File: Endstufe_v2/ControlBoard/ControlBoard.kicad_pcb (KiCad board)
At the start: 2 copper layers, 67 parts, among them J1 Conn_01x02_Pin, J3 DNP, J7 DNP, SW1 TS-1187A-B-A-B, SW2 TS-1187A-B-A-B, U1 TPS62933, U2 TYPE-C 16PFS 2JCB1.2-H6.5 IPX8, U3 W25Q128JVS, U4 RP2040, U5 NVTFWS014P04M8LTAG, U6 1SMA5927A, U7 ADAU1463WBCPZ300, Y1 12Mhz

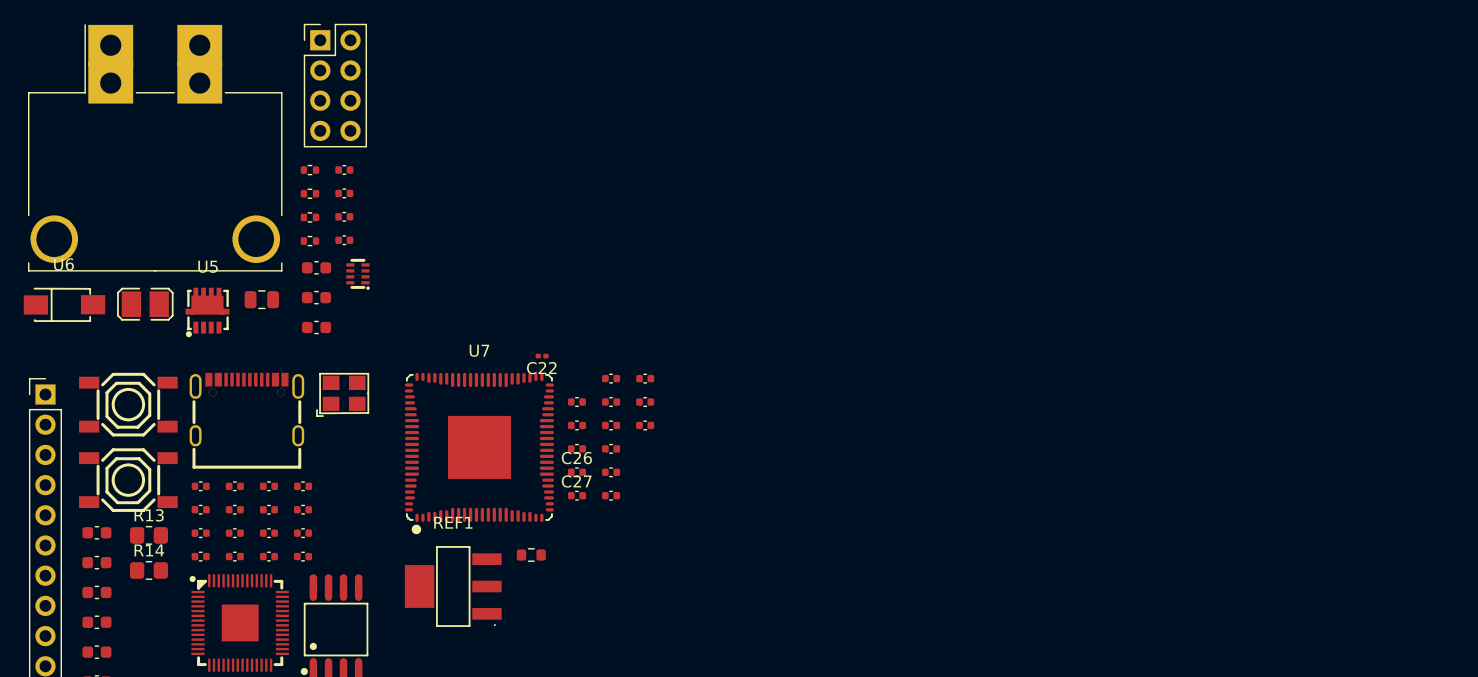
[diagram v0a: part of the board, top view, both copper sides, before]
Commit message: Added ADAU1962A DAC schematic
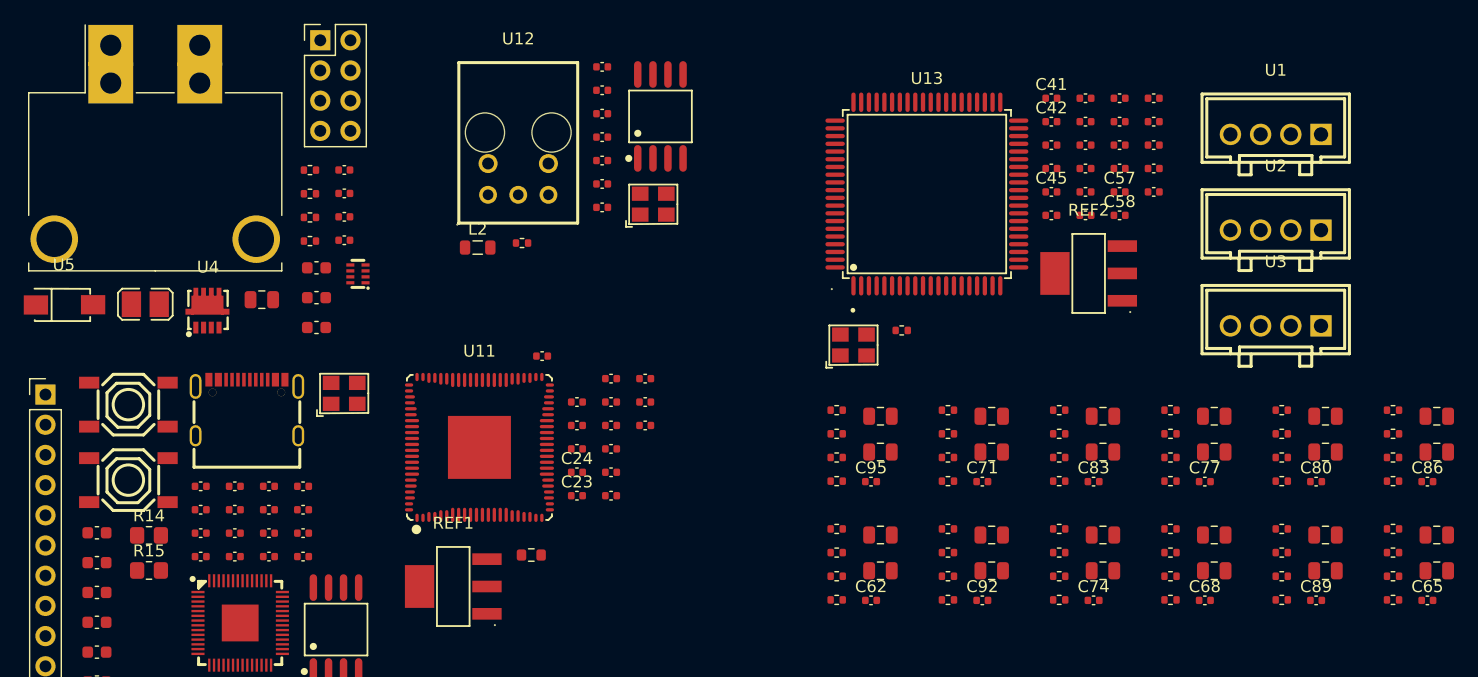
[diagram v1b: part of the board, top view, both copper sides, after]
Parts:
- added C22: 10uF, Endstufe:C_0402_1005Metric, F.Cu at (103.5, 66.6)
- added C25: 30pF, Endstufe:C_0402_1005Metric, F.Cu at (103.5, 62.6)
- added C26: 30pF, Endstufe:C_0402_1005Metric, F.Cu at (103.5, 64.6)
- added C35: 100nF, Endstufe:C_0402_1005Metric, F.Cu at (103.5, 60.7)
- added C41: 470nF, Capacitor_SMD:C_0402_1005Metric, F.Cu at (141.3, 63.3)
- added C42: 470nF, Capacitor_SMD:C_0402_1005Metric, F.Cu at (141.3, 65.3)
- added C43: 30pF, Endstufe:C_0402_1005Metric, F.Cu at (141.3, 67.2)
- added C44: 30pF, Endstufe:C_0402_1005Metric, F.Cu at (141.3, 69.2)
- added C45: 5.6nF, Capacitor_SMD:C_0402_1005Metric, F.Cu at (141.3, 71.2)
- added C46: 10uF, Endstufe:C_0402_1005Metric, F.Cu at (141.3, 73.2)
- added C47: 10uF, Endstufe:C_0402_1005Metric, F.Cu at (144.2, 63.3)
- added C48: 10uF, Endstufe:C_0402_1005Metric, F.Cu at (144.2, 65.3)
- added C49: 10uF, Endstufe:C_0402_1005Metric, F.Cu at (144.2, 67.2)
- added C50: 10uF, Endstufe:C_0402_1005Metric, F.Cu at (144.2, 69.2)
- added C51: 10uF, Endstufe:C_0402_1005Metric, F.Cu at (144.2, 71.2)
- added C52: 10uF, Endstufe:C_0402_1005Metric, F.Cu at (144.2, 73.2)
- added C53: 10uF, Endstufe:C_0402_1005Metric, F.Cu at (147.1, 63.3)
- added C54: 10uF, Endstufe:C_0402_1005Metric, F.Cu at (147.1, 65.3)
- added C55: 10uF, Endstufe:C_0402_1005Metric, F.Cu at (147.1, 67.2)
- added C56: 10uF, Endstufe:C_0402_1005Metric, F.Cu at (147.1, 69.2)
- added C57: 470nF, Capacitor_SMD:C_0402_1005Metric, F.Cu at (147.1, 71.2)
- added C58: 470nF, Capacitor_SMD:C_0402_1005Metric, F.Cu at (147.1, 73.2)
- added C59: 10uF, Endstufe:C_0402_1005Metric, F.Cu at (149.9, 63.3)
- added C60: 10uF, Endstufe:C_0402_1005Metric, F.Cu at (149.9, 65.3)
- added C61: 10uF, Endstufe:C_0402_1005Metric, F.Cu at (149.9, 67.2)
- added C62: 2.7nF, Capacitor_SMD:C_0402_1005Metric, F.Cu at (126.2, 105.5)
- added C63: 10uF, Endstufe:C_0805_2012Metric, F.Cu at (127.0, 100.0)
- added C64: 10uF, Endstufe:C_0805_2012Metric, F.Cu at (127.0, 103.1)
- added C65: 2.7nF, Capacitor_SMD:C_0402_1005Metric, F.Cu at (173.0, 105.5)
- added C66: 10uF, Endstufe:C_0805_2012Metric, F.Cu at (173.8, 100.0)
- added C67: 10uF, Endstufe:C_0805_2012Metric, F.Cu at (173.8, 103.1)
- added C68: 2.7nF, Capacitor_SMD:C_0402_1005Metric, F.Cu at (154.2, 105.5)
- added C69: 10uF, Endstufe:C_0805_2012Metric, F.Cu at (155.0, 100.0)
- added C70: 10uF, Endstufe:C_0805_2012Metric, F.Cu at (155.0, 103.1)
- added C71: 2.7nF, Capacitor_SMD:C_0402_1005Metric, F.Cu at (135.5, 95.6)
- added C72: 10uF, Endstufe:C_0805_2012Metric, F.Cu at (136.3, 90.1)
- added C73: 10uF, Endstufe:C_0805_2012Metric, F.Cu at (136.3, 93.1)
- added C74: 2.7nF, Capacitor_SMD:C_0402_1005Metric, F.Cu at (144.9, 105.5)
- added C75: 10uF, Endstufe:C_0805_2012Metric, F.Cu at (145.7, 100.0)
- added C76: 10uF, Endstufe:C_0805_2012Metric, F.Cu at (145.7, 103.1)
- added C77: 2.7nF, Capacitor_SMD:C_0402_1005Metric, F.Cu at (154.2, 95.6)
- added C78: 10uF, Endstufe:C_0805_2012Metric, F.Cu at (155.0, 90.1)
- added C79: 10uF, Endstufe:C_0805_2012Metric, F.Cu at (155.0, 93.1)
- added C80: 2.7nF, Capacitor_SMD:C_0402_1005Metric, F.Cu at (163.6, 95.6)
- added C81: 10uF, Endstufe:C_0805_2012Metric, F.Cu at (164.4, 90.1)
- added C82: 10uF, Endstufe:C_0805_2012Metric, F.Cu at (164.4, 93.1)
- added C83: 2.7nF, Capacitor_SMD:C_0402_1005Metric, F.Cu at (144.9, 95.6)
- added C84: 10uF, Endstufe:C_0805_2012Metric, F.Cu at (145.7, 90.1)
- added C85: 10uF, Endstufe:C_0805_2012Metric, F.Cu at (145.7, 93.1)
- added C86: 2.7nF, Capacitor_SMD:C_0402_1005Metric, F.Cu at (173.0, 95.6)
- added C87: 10uF, Endstufe:C_0805_2012Metric, F.Cu at (173.8, 90.1)
- added C88: 10uF, Endstufe:C_0805_2012Metric, F.Cu at (173.8, 93.1)
- added C89: 2.7nF, Capacitor_SMD:C_0402_1005Metric, F.Cu at (163.6, 105.5)
- added C90: 10uF, Endstufe:C_0805_2012Metric, F.Cu at (164.4, 100.0)
- added C91: 10uF, Endstufe:C_0805_2012Metric, F.Cu at (164.4, 103.1)
- added C92: 2.7nF, Capacitor_SMD:C_0402_1005Metric, F.Cu at (135.5, 105.5)
- added C93: 10uF, Endstufe:C_0805_2012Metric, F.Cu at (136.3, 100.0)
- added C94: 10uF, Endstufe:C_0805_2012Metric, F.Cu at (136.3, 103.1)
- added C95: 2.7nF, Capacitor_SMD:C_0402_1005Metric, F.Cu at (126.2, 95.6)
- added C96: 10uF, Endstufe:C_0805_2012Metric, F.Cu at (127.0, 90.1)
- added C97: 10uF, Endstufe:C_0805_2012Metric, F.Cu at (127.0, 93.1)
- added L2: 47uH, Inductor_SMD:L_0805_2012Metric, F.Cu at (93.1, 75.9)
- added R16: 10k, Endstufe:C_0402_1005Metric, F.Cu at (103.5, 72.5)
- added R19: 100, Endstufe:R_0402_1005Metric, F.Cu at (96.8, 75.5)
- added R20: 10k, Endstufe:C_0402_1005Metric, F.Cu at (103.5, 68.5)
- added R21: 10k, Endstufe:C_0402_1005Metric, F.Cu at (103.5, 70.5)
- added R23: 1k, Endstufe:C_0402_1005Metric, F.Cu at (149.9, 69.2)
- added R24: 100, Endstufe:R_0402_1005Metric, F.Cu at (128.8, 82.8)
- added R25: 10k, Endstufe:C_0402_1005Metric, F.Cu at (149.9, 71.2)
- added R26: 237, Endstufe:R_0402_1005Metric, F.Cu at (123.3, 99.5)
- added R27: 237, Endstufe:R_0402_1005Metric, F.Cu at (123.3, 101.5)
- added R28: 49.9k, Endstufe:R_0402_1005Metric, F.Cu at (123.3, 103.5)
- added R29: 49.9k, Endstufe:R_0402_1005Metric, F.Cu at (123.3, 105.5)
- added R30: 237, Endstufe:R_0402_1005Metric, F.Cu at (170.1, 99.5)
- added R31: 237, Endstufe:R_0402_1005Metric, F.Cu at (170.1, 101.5)
- added R32: 49.9k, Endstufe:R_0402_1005Metric, F.Cu at (170.1, 103.5)
- added R33: 49.9k, Endstufe:R_0402_1005Metric, F.Cu at (170.1, 105.5)
- added R34: 237, Endstufe:R_0402_1005Metric, F.Cu at (151.4, 99.5)
- added R35: 237, Endstufe:R_0402_1005Metric, F.Cu at (151.4, 101.5)
- added R36: 49.9k, Endstufe:R_0402_1005Metric, F.Cu at (151.4, 103.5)
- added R37: 49.9k, Endstufe:R_0402_1005Metric, F.Cu at (151.4, 105.5)
- added R38: 237, Endstufe:R_0402_1005Metric, F.Cu at (132.6, 89.5)
- added R39: 237, Endstufe:R_0402_1005Metric, F.Cu at (132.6, 91.5)
- added R40: 49.9k, Endstufe:R_0402_1005Metric, F.Cu at (132.6, 93.5)
- added R41: 49.9k, Endstufe:R_0402_1005Metric, F.Cu at (132.6, 95.5)
- added R42: 237, Endstufe:R_0402_1005Metric, F.Cu at (142.0, 99.5)
- added R43: 237, Endstufe:R_0402_1005Metric, F.Cu at (142.0, 101.5)
- added R44: 49.9k, Endstufe:R_0402_1005Metric, F.Cu at (142.0, 103.5)
- added R45: 49.9k, Endstufe:R_0402_1005Metric, F.Cu at (142.0, 105.5)
- added R46: 237, Endstufe:R_0402_1005Metric, F.Cu at (151.4, 89.5)
- added R47: 237, Endstufe:R_0402_1005Metric, F.Cu at (151.4, 91.5)
- added R48: 49.9k, Endstufe:R_0402_1005Metric, F.Cu at (151.4, 93.5)
- added R49: 49.9k, Endstufe:R_0402_1005Metric, F.Cu at (151.4, 95.5)
- added R50: 237, Endstufe:R_0402_1005Metric, F.Cu at (160.7, 89.5)
- added R51: 237, Endstufe:R_0402_1005Metric, F.Cu at (160.7, 91.5)
- added R52: 49.9k, Endstufe:R_0402_1005Metric, F.Cu at (160.7, 93.5)
- added R53: 49.9k, Endstufe:R_0402_1005Metric, F.Cu at (160.7, 95.5)
- added R54: 237, Endstufe:R_0402_1005Metric, F.Cu at (142.0, 89.5)
- added R55: 237, Endstufe:R_0402_1005Metric, F.Cu at (142.0, 91.5)
- added R56: 49.9k, Endstufe:R_0402_1005Metric, F.Cu at (142.0, 93.5)
- added R57: 49.9k, Endstufe:R_0402_1005Metric, F.Cu at (142.0, 95.5)
- added R58: 237, Endstufe:R_0402_1005Metric, F.Cu at (170.1, 89.5)
- added R59: 237, Endstufe:R_0402_1005Metric, F.Cu at (170.1, 91.5)
- added R60: 49.9k, Endstufe:R_0402_1005Metric, F.Cu at (170.1, 93.5)
- added R61: 49.9k, Endstufe:R_0402_1005Metric, F.Cu at (170.1, 95.5)
- added R62: 237, Endstufe:R_0402_1005Metric, F.Cu at (160.7, 99.5)
- added R63: 237, Endstufe:R_0402_1005Metric, F.Cu at (160.7, 101.5)
- added R64: 49.9k, Endstufe:R_0402_1005Metric, F.Cu at (160.7, 103.5)
- added R65: 49.9k, Endstufe:R_0402_1005Metric, F.Cu at (160.7, 105.5)
- added R66: 237, Endstufe:R_0402_1005Metric, F.Cu at (132.6, 99.5)
- added R67: 237, Endstufe:R_0402_1005Metric, F.Cu at (132.6, 101.5)
- added R68: 49.9k, Endstufe:R_0402_1005Metric, F.Cu at (132.6, 103.5)
- added R69: 49.9k, Endstufe:R_0402_1005Metric, F.Cu at (132.6, 105.5)
- added R70: 237, Endstufe:R_0402_1005Metric, F.Cu at (123.3, 89.5)
- added R71: 237, Endstufe:R_0402_1005Metric, F.Cu at (123.3, 91.5)
- added R72: 49.9k, Endstufe:R_0402_1005Metric, F.Cu at (123.3, 93.5)
- added R73: 49.9k, Endstufe:R_0402_1005Metric, F.Cu at (123.3, 95.5)
- added REF2: FZT792ATA, Endstufe:SOT-223-4_L6.5-W3.5-P2.30-LS7.0-BR, F.Cu at (144.5, 78.0)
- added U1: B4B-XH-2_(LF)(SN), Endstufe:CONN-TH_B4B-XH-2-LF-SN, F.Cu at (160.2, 66.4)
- added U10: W25Q128JVS, Endstufe:SOIC-8_L5.3-W5.3-P1.27-LS8.0-BL, F.Cu at (108.5, 64.8)
- added U12: ZPLR135_T8, Endstufe:CONN-TH_ZPLR135-T8, F.Cu at (96.5, 70.1)
- added U13: ADAU1962AWBSTZ, Endstufe:LQFP-80_L14.0-W14.0-P0.65-LS16.0-BL, F.Cu at (130.9, 71.4)
- added U2: B4B-XH-2_(LF)(SN), Endstufe:CONN-TH_B4B-XH-2-LF-SN, F.Cu at (160.2, 74.4)
- added U3: B4B-XH-2_(LF)(SN), Endstufe:CONN-TH_B4B-XH-2-LF-SN, F.Cu at (160.2, 82.5)
- added Y2: 24.576Mhz, Endstufe:OSC-SMD_4P-L3.2-W2.5-BL, F.Cu at (107.8, 72.2)
- added Y3: 24.576Mhz, Endstufe:OSC-SMD_4P-L3.2-W2.5-BL, F.Cu at (124.7, 84.1)
- C38: renamed from C22; footprint Capacitor_SMD:C_0201_0603Metric -> Endstufe:C_0402_1005Metric
- renumbered C27 to C23, C26 to C24, C35 to C27, C29 to C28, C31 to C29, C34 to C30, C30 to C31, C23 to C32, C25 to C33, C28 to C34, C24 to C36, C32 to C37, C33 to C39, J1 to J2, J7 to J5, R9 to R10, R10 to R11, R11 to R12, R12 to R13, R13 to R14, R14 to R15, R16 to R17, R17 to R18, R15 to R2, R2 to R3, R3 to R4, R4 to R5, R5 to R6, R6 to R7, R7 to R8, R8 to R9, U7 to U11, U5 to U4, U6 to U5, U1 to U6, U2 to U7, U3 to U8, U4 to U9
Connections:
- U11 pad 10: unconnected-(U7-AUXADC0-Pad10) -> /ADAU1463/AUXADC0
- U11 pad 11: unconnected-(U7-AUXADC1-Pad11) -> /ADAU1463/AUXADC1
- U11 pad 12: unconnected-(U7-AUXADC2-Pad12) -> Net-(U11-AUXADC2)
- U11 pad 25: unconnected-(U7-XTALIN/MCLK-Pad25) -> Net-(U11-XTALIN/MCLK)
- U11 pad 26: unconnected-(U7-XTALOUT-Pad26) -> Net-(U11-XTALOUT)
- U11 pad 27: unconnected-(U7-CLKOUT-Pad27) -> Net-(U11-CLKOUT)
- U11 pad 28: unconnected-(U7-RESET#-Pad28) -> /ADAU1463/RESET
- U11 pad 32: unconnected-(U7-SS_M/MP0-Pad32) -> /ADAU1463/SPI_SS
- U11 pad 33: unconnected-(U7-MOSI_M/MP1-Pad33) -> /ADAU1463/SPI_MOSI
- U11 pad 34: unconnected-(U7-SCL_M/SCLK_M/MP2-Pad34) -> /ADAU1463/SPI_SCLK
- U11 pad 35: unconnected-(U7-SDA_M/MISO_M/MP3-Pad35) -> /ADAU1463/SPI_MISO
- U11 pad 38: unconnected-(U7-MISO/SDA-Pad38) -> /ADAU1463/SDA
- U11 pad 39: unconnected-(U7-SCLK/SCL-Pad39) -> /ADAU1463/SCL
- U11 pad 4: unconnected-(U7-SPDIFIN-Pad4) -> /ADAU1463/SPDIFIN
- U11 pad 40: unconnected-(U7-MOSI/ADDR1-Pad40) -> /ADAU1463/ADDR1
- U11 pad 41: unconnected-(U7-SS/ADDR0-Pad41) -> /ADAU1463/ADDR0
- U11 pad 42: unconnected-(U7-SELFBOOT-Pad42) -> Net-(U11-SELFBOOT)
- U11 pad 47: unconnected-(U7-LRCLK_OUT0/MP4-Pad47) -> Net-(J8-Pin_2)
- U11 pad 48: unconnected-(U7-BCLK_OUT0-Pad48) -> Net-(J8-Pin_3)
- U11 pad 49: unconnected-(U7-SDATA_OUT0-Pad49) -> Net-(J8-Pin_4)
- U11 pad 50: unconnected-(U7-LRCLK_OUT1/MP5-Pad50) -> /ADAU1463/DAC_LRCLK
- U11 pad 51: unconnected-(U7-BCLK_OUT1-Pad51) -> /ADAU1463/DAC_BLCK
- U11 pad 52: unconnected-(U7-SDATA_OUT1-Pad52) -> /ADAU1463/DAC_DATA0
- U11 pad 61: unconnected-(U7-SDATAIO7/MP23-Pad61) -> /ADAU1463/DAC_DATA1
- U11 pad 62: unconnected-(U7-SDATAIO6/MP22-Pad62) -> /ADAU1463/DAC_DATA2
- U11 pad 69: unconnected-(U7-SDATAIO3/MP19-Pad69) -> Net-(J7-Pin_1)
- U11 pad 70: unconnected-(U7-SDATAIO2/MP18-Pad70) -> Net-(J7-Pin_2)
- U11 pad 71: unconnected-(U7-SDATAIO1/MP17-Pad71) -> Net-(J7-Pin_3)
- U11 pad 72: unconnected-(U7-SDATAIO0/MP16-Pad72) -> Net-(J7-Pin_4)
- U11 pad 73: unconnected-(U7-BCLK_IN0-Pad73) -> /ADAU1463/ADDITIONAL_BLCK
- U11 pad 74: unconnected-(U7-LRCLK_IN0/MP10-Pad74) -> /ADAU1463/ADDITIONAL_LRCLK
- U11 pad 75: unconnected-(U7-SDATA_IN0-Pad75) -> /ADAU1463/ADDITIONAL_SDATA
- U11 pad 79: unconnected-(U7-THD_M-Pad79) -> Net-(U11-THD_M)
- U11 pad 80: unconnected-(U7-THD_P-Pad80) -> Net-(U11-THD_P)
- U11 pad 81: unconnected-(U7-BCLK_IN2-Pad81) -> /ADAU1463/PCM9211_BLCK
- U11 pad 82: unconnected-(U7-LRCLK_IN2/MP12-Pad82) -> /ADAU1463/PCM9211_LRCLK
- U11 pad 83: unconnected-(U7-SDATA_IN2-Pad83) -> /ADAU1463/PCM9211_SDATA
- U11 pad 84: unconnected-(U7-BCLK_IN3-Pad84) -> /ADAU1463/PCM1865_BLCK
- U11 pad 85: unconnected-(U7-LRCLK_IN3/MP13-Pad85) -> /ADAU1463/PCM1865_LRCLK
- U11 pad 86: unconnected-(U7-SDATA_IN3-Pad86) -> /ADAU1463/PCM1865_SDATA

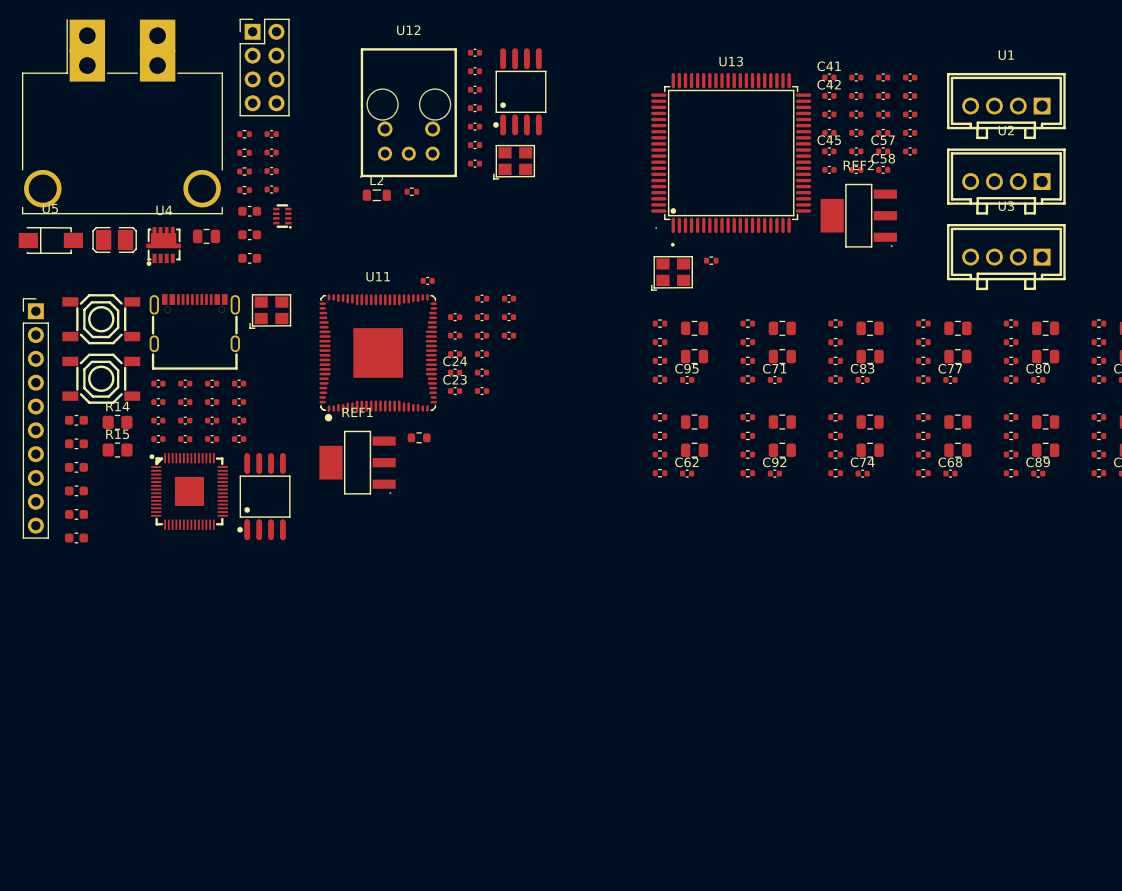
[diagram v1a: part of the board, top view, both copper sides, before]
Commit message: Add footprints to all components
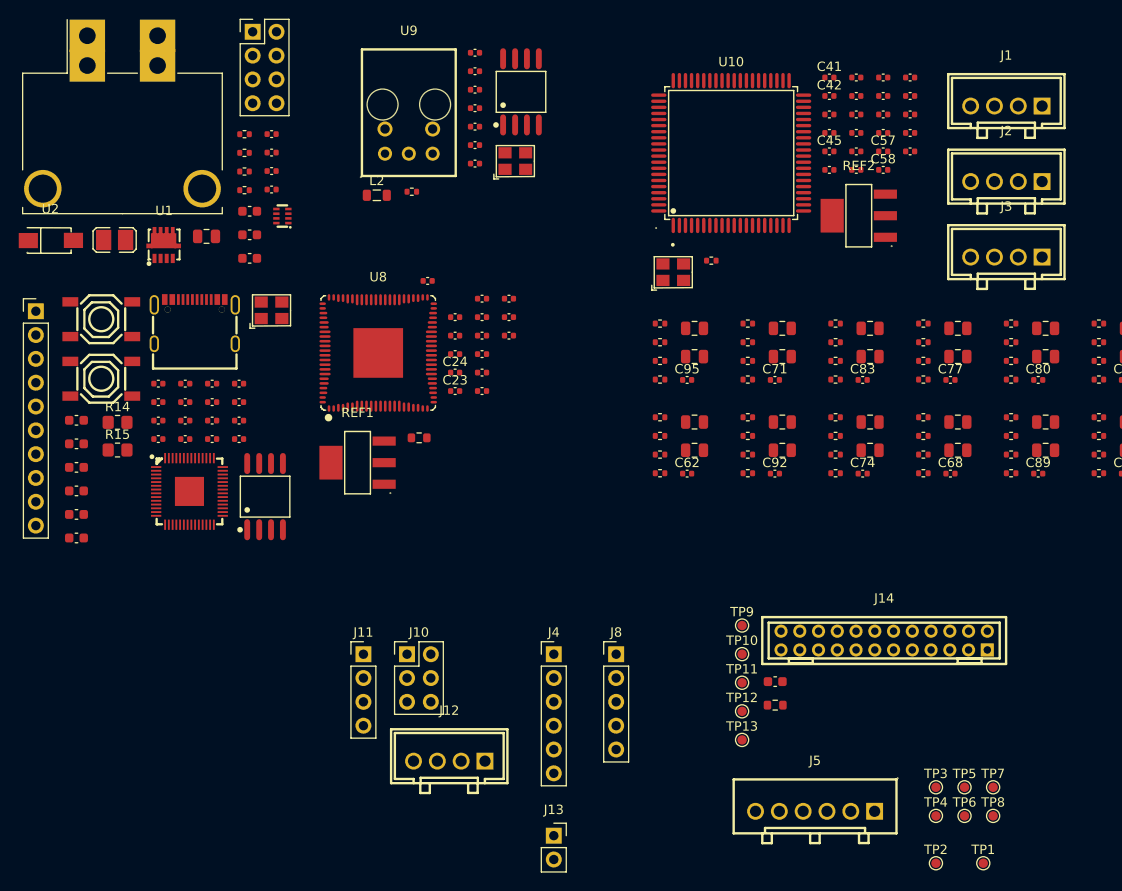
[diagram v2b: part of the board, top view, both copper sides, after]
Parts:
- added C40: 390pF, Endstufe:C_0603_1608Metric, F.Cu at (135.6, 127.7)
- added J10: DNP, Connector_PinHeader_2.54mm:PinHeader_2x03_P2.54mm_Vertical, F.Cu at (96.3, 124.8)
- added J11: DNP, Connector_PinHeader_2.54mm:PinHeader_1x04_P2.54mm_Vertical, F.Cu at (91.7, 124.8)
- added J12: DNP, Endstufe:CONN-TH_B4B-XH-2-LF-SN, F.Cu at (100.8, 136.2)
- added J13: DNP, Connector_PinSocket_2.54mm:PinSocket_1x02_P2.54mm_Vertical, F.Cu at (112.0, 144.2)
- added J14: DAC all outputs, Endstufe:CONN-TH_24P-P2.00_B24B-PHDSS, F.Cu at (147.2, 123.4)
- added J4: DNP, Connector_PinHeader_2.54mm:PinHeader_1x06_P2.54mm_Vertical, F.Cu at (112.0, 124.8)
- added J5: B6B-XH-2(LF)(SN), Endstufe:CONN-TH_B6B-XH-2-LF-SN, F.Cu at (139.8, 141.6)
- added J8: DNP, Connector_PinHeader_2.54mm:PinHeader_1x05_P2.54mm_Vertical, F.Cu at (118.6, 124.8)
- added R22: 562, Endstufe:R_0603_1608Metric, F.Cu at (135.6, 130.2)
- added TP1: TestPoint, TestPoint:TestPoint_Pad_D1.0mm, F.Cu at (157.8, 147.1)
- added TP10: TestPoint, TestPoint:TestPoint_Pad_D1.0mm, F.Cu at (132.0, 124.8)
- added TP11: TestPoint, TestPoint:TestPoint_Pad_D1.0mm, F.Cu at (132.0, 127.8)
- added TP12: TestPoint, TestPoint:TestPoint_Pad_D1.0mm, F.Cu at (132.0, 130.9)
- added TP13: TestPoint, TestPoint:TestPoint_Pad_D1.0mm, F.Cu at (132.0, 133.9)
- added TP2: TestPoint, TestPoint:TestPoint_Pad_D1.0mm, F.Cu at (152.7, 147.1)
- added TP3: TestPoint, TestPoint:TestPoint_Pad_D1.0mm, F.Cu at (152.7, 139.0)
- added TP4: TestPoint, TestPoint:TestPoint_Pad_D1.0mm, F.Cu at (152.7, 142.1)
- added TP5: TestPoint, TestPoint:TestPoint_Pad_D1.0mm, F.Cu at (155.8, 139.0)
- added TP6: TestPoint, TestPoint:TestPoint_Pad_D1.0mm, F.Cu at (155.8, 142.1)
- added TP7: TestPoint, TestPoint:TestPoint_Pad_D1.0mm, F.Cu at (158.8, 139.0)
- added TP8: TestPoint, TestPoint:TestPoint_Pad_D1.0mm, F.Cu at (158.8, 142.1)
- added TP9: TestPoint, TestPoint:TestPoint_Pad_D1.0mm, F.Cu at (132.0, 121.8)
- renumbered U1 to J1, U2 to J2, U3 to J3, J2 to J6, J3 to J7, J5 to J9, U4 to U1, U13 to U10, U5 to U2, U6 to U3, U7 to U4, U8 to U5, U9 to U6, U10 to U7, U11 to U8, U12 to U9
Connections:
- net /ADAU1962A/DAC_Filter10/OUTPUTxN renamed /ADAU1962A/DAC2N
- net /ADAU1962A/DAC_Filter10/OUTPUTxP renamed /ADAU1962A/DAC2P
- net /ADAU1962A/DAC_Filter11/OUTPUTxN renamed /ADAU1962A/DAC1N
- net /ADAU1962A/DAC_Filter11/OUTPUTxP renamed /ADAU1962A/DAC1P
- net /ADAU1962A/DAC_Filter9/OUTPUTxN renamed /ADAU1962A/DAC3N
- net /ADAU1962A/DAC_Filter9/OUTPUTxP renamed /ADAU1962A/DAC3P
- U10 pad 27: /ADAU1962A/BCLK -> /ADAU1463/DAC_BLCK
- U10 pad 28: /ADAU1962A/LRCLK -> /ADAU1463/DAC_LRCLK
- U10 pad 36: /ADAU1962A/SDATA3 -> /ADAU1463/DAC_DATA2
- U10 pad 37: /ADAU1962A/SDATA2 -> /ADAU1463/DAC_DATA1
- U10 pad 38: /ADAU1962A/SDATA1 -> /ADAU1463/DAC_DATA0
- U8 pad 89: unconnected-(U11-EP-Pad89) -> GND

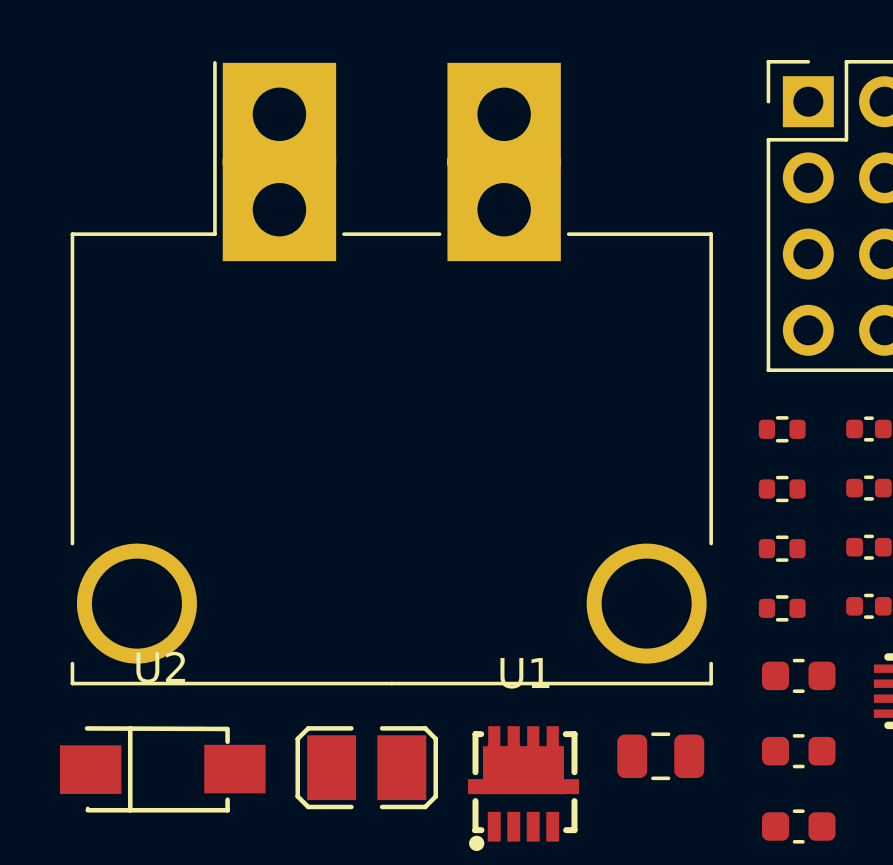
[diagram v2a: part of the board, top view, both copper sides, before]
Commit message: Fix connector footprints
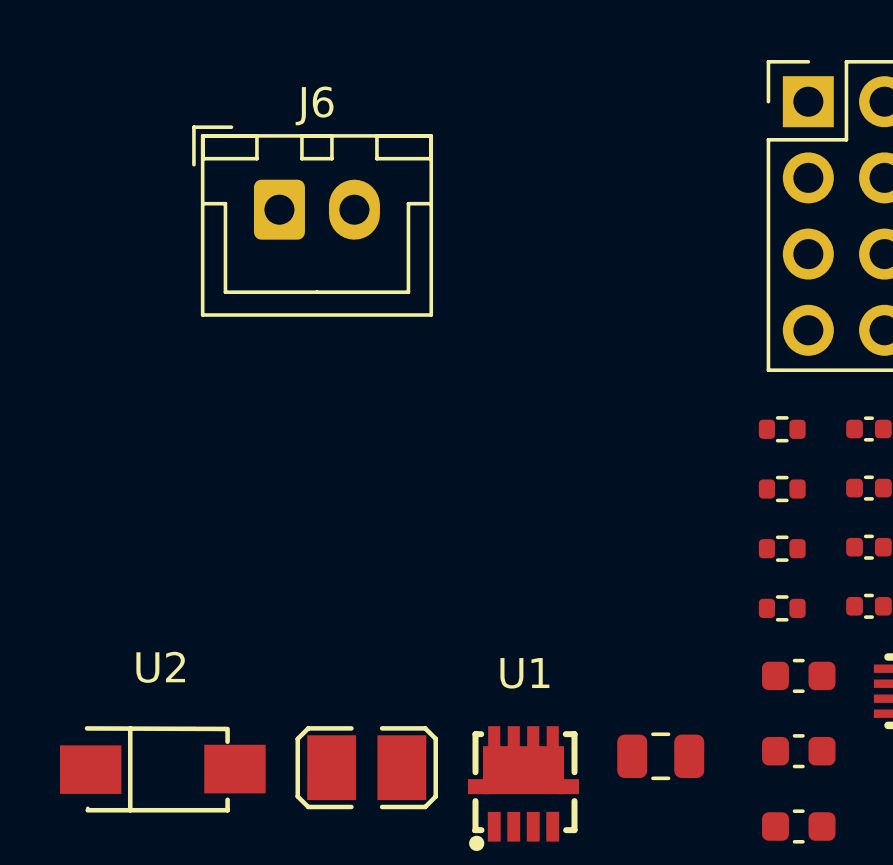
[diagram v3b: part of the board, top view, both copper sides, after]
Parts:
- J6: footprint Endstufe:Molex_Sabre_43160-1102_1x02_P7.49mm_Horizontal -> Connector_JST:JST_XH_B2B-XH-A_1x02_P2.50mm_Vertical
